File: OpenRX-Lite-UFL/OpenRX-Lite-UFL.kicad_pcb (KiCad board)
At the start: 6 copper layers, 8.5 x 12.3 mm, 39 parts, among them U1 ESP32-C3FH4, U2 TLV75533PDQNR, U3 SX1281IMLTRT, X1 CJ17-400001010B20

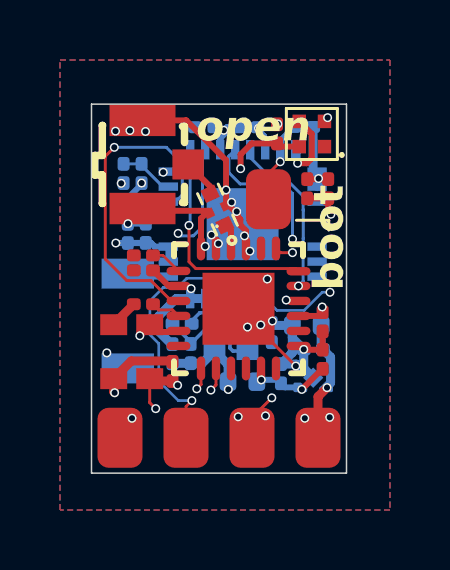
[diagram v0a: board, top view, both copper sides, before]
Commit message: switch to 0.2mm vias
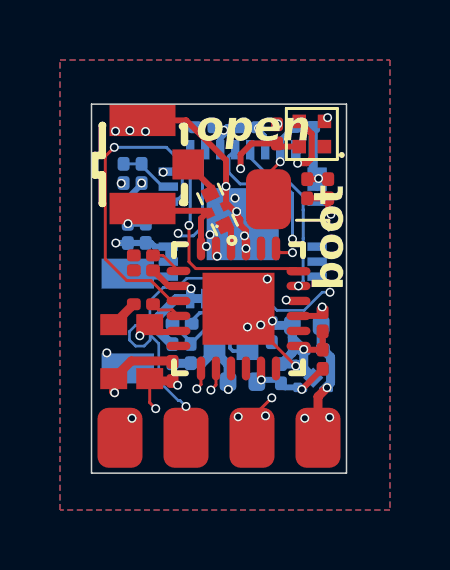
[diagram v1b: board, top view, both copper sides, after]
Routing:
- net Net-(U1-U0TXD): track 9.68 -> 11.3 mm
